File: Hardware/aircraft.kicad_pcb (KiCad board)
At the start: 4 copper layers, 100 x 50 mm, 190 parts, among them J1 Conn_01x02_Pin, J12 Conn_02x05_Odd_Even, J13 Conn_01x02, J14 USB_B_Micro, J15 Conn_02x05_Odd_Even, J16 USB_B_Micro, J17 USB_B_Micro, J18 USB_B_Micro, J19 U.FL-R-SMT-1_80_, J2 DM3AT-SF-PEJM5, J3 Conn_01x04, J4 Conn_01x04, J5 Conn_02x10_Odd_Even, J6 Conn_01x10, J7 Conn_01x04, J8 Conn_01x04, SW1 SW_SPDT, SW2 SW_Push_Dual, SW3 SW_SPDT, SW4 SW_Push_Dual, U1 MIC26903YJL-TR, U10 BMP390, U11 W25N01GVZEIG_TR, U12 STM32F405RGTx, U13 W25N01GVZEIG_TR, U14 24CW1280T-I/OT, U15 PCA9685PW_118, U16 CH330N, U17 CH330N, U2 LD39200PU33R, U3 INA226, U4 STM32F405RGTx, U5 IST8310, U6 NEO-M8N, U7 BMI088, U8 TMP100, U9 24CW1280T-I/OT, Y1 25MHz, Y2 25MHz

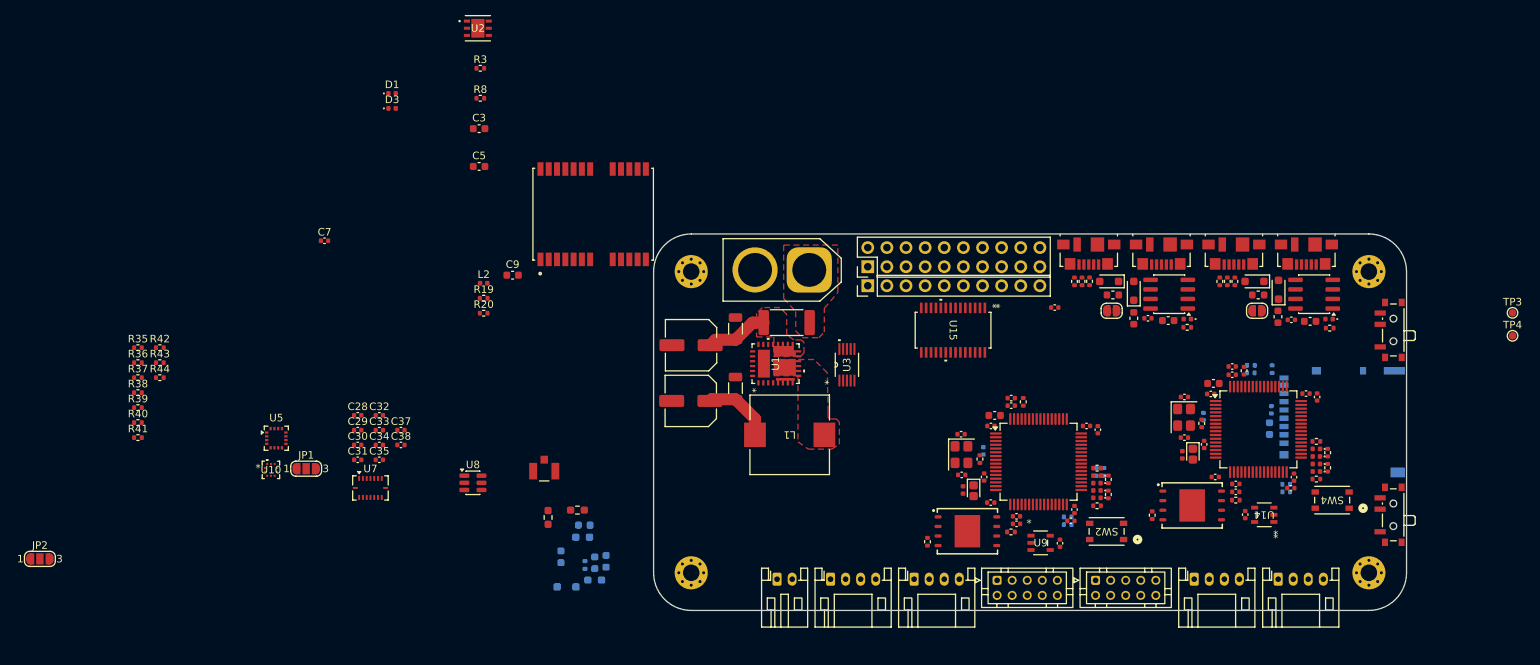
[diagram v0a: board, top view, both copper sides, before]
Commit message: fill zones done, layout reformulation because of 5v, power supply power traces done
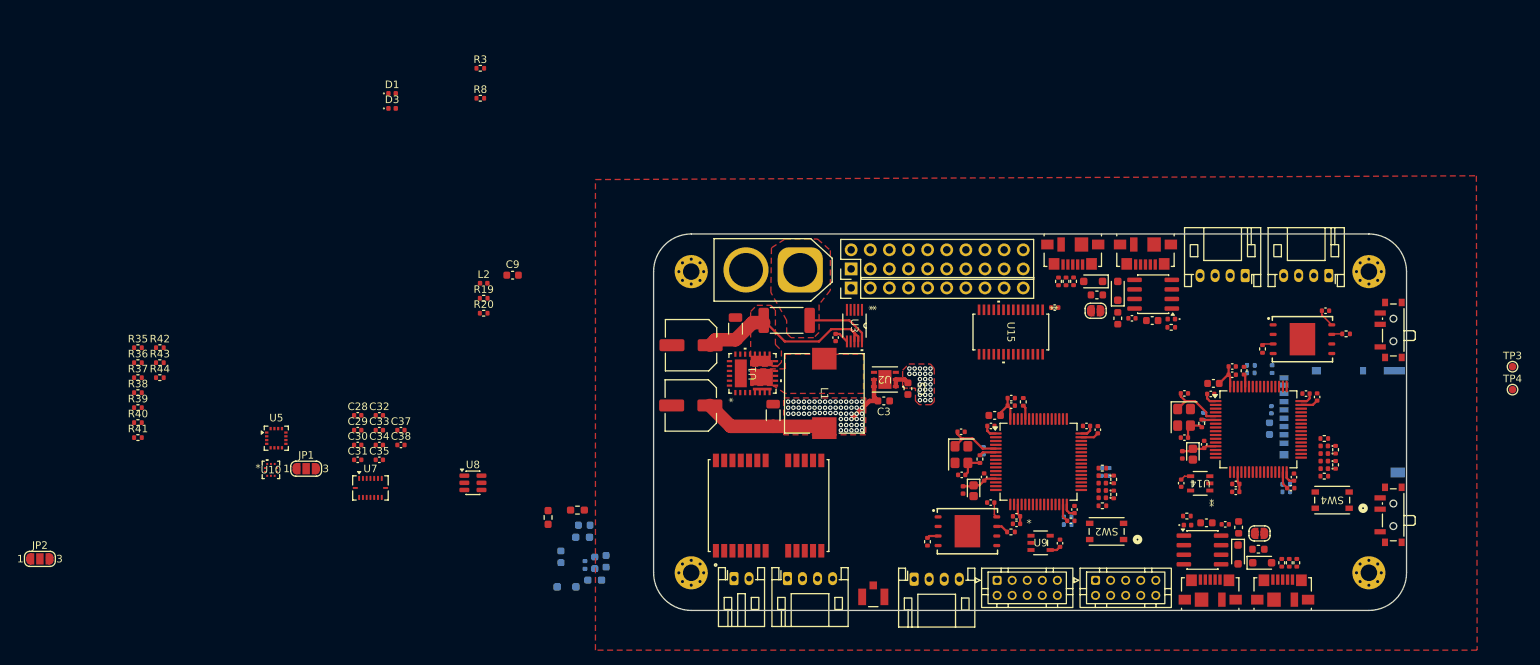
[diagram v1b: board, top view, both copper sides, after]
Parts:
- moved U2 71.4 mm to (149.4, 70.0), turned to 180 degrees
- moved C7 69.1 mm to (142.9, 64.5), turned to -90 degrees
- moved C3 64.8 mm to (149.3, 72.9), turned to 180 degrees
- moved C5 64.1 mm to (152.5, 71.3), turned to -90 degrees
- moved J19 46.8 mm to (147.9, 98.9)
- moved J14 46.6 mm to (192.7, 98.1), turned to 0 degrees
- moved J16 45.2 mm to (202.3, 98.1), turned to 0 degrees
- moved U6 45.2 mm to (134.0, 86.8)
- moved J8 44.1 mm to (208.4, 56.2), turned to 180 degrees
- moved J7 40.6 mm to (197.3, 56.2), turned to 180 degrees
- moved R48 38.7 mm to (204.2, 94.4), turned to 90 degrees
- moved R46 38.3 mm to (203.2, 94.4), turned to 90 degrees
- moved R47 37.9 mm to (202.2, 94.4), turned to 90 degrees
- moved D13 37.4 mm to (199.6, 94.4), turned to 0 degrees
- moved U16 37.1 mm to (191.6, 92.7), turned to 0 degrees
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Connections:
- U15 pad 10: PWM_4 -> unconnected-(U15-LED4-Pad10)
- U15 pad 11: PWM_5 -> unconnected-(U15-LED5-Pad11)
- U15 pad 12: PWM_6 -> unconnected-(U15-LED6-Pad12)
- U15 pad 13: PWM_7 -> unconnected-(U15-LED7-Pad13)
- U15 pad 15: PWM_8 -> unconnected-(U15-LED8-Pad15)
- U15 pad 16: PWM_9 -> unconnected-(U15-LED9-Pad16)
- U15 pad 6: PWM_0 -> PWM_3
- U15 pad 7: PWM_1 -> PWM_2
- U15 pad 8: PWM_2 -> PWM_1
- U15 pad 9: PWM_3 -> PWM_0
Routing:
- net +3.3V: track 0.29 -> 36.1 mm, vias 0 -> 25
- net PS_PVIN: track 8.36 -> 25.6 mm
- net +5V: track 9.29 -> 25.9 mm, vias 0 -> 60
- net VIN+: track 0.00 -> 8.77 mm
- net FCU_OSC_IN: track 0.00 -> 7.90 mm
- net NU_OSC_IN: track 0.00 -> 7.68 mm
- net NU_VDDA: track 0.00 -> 4.77 mm
- net FCU_VDDA: track 0.00 -> 4.69 mm
- net Net-(C18-Pad1): track 0.00 -> 3.34 mm
- net Net-(C46-Pad1): track 0.00 -> 3.32 mm
- net Net-(U4-VCAP_2): track 0.00 -> 2.42 mm
- net Net-(U4-VCAP_1): track 0.00 -> 2.41 mm
- net Net-(U12-VCAP_2): track 0.00 -> 2.36 mm
- net Net-(U12-VCAP_1): track 0.00 -> 2.36 mm
- net NU_OSC_OUT: track 0.00 -> 2.27 mm
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- added copper zone on F.Cu, net +3.3V
- added copper zone on In2.Cu, net +3.3V
- added copper zone on F.Cu, net +5V
- added copper zone on In2.Cu, net +5V
- added copper zone on F.Cu, net GND
- added copper zone on In1.Cu, net GND
